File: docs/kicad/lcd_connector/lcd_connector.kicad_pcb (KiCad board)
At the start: 2 copper layers, 20.3 x 38.1 mm, 19 parts, among them J1 5V, J2 T_CS, J3 CLK, J4 MISO, J5 DC, J6 CS, J7 MOSI, J8 GND, M1 TFT_ILI9341

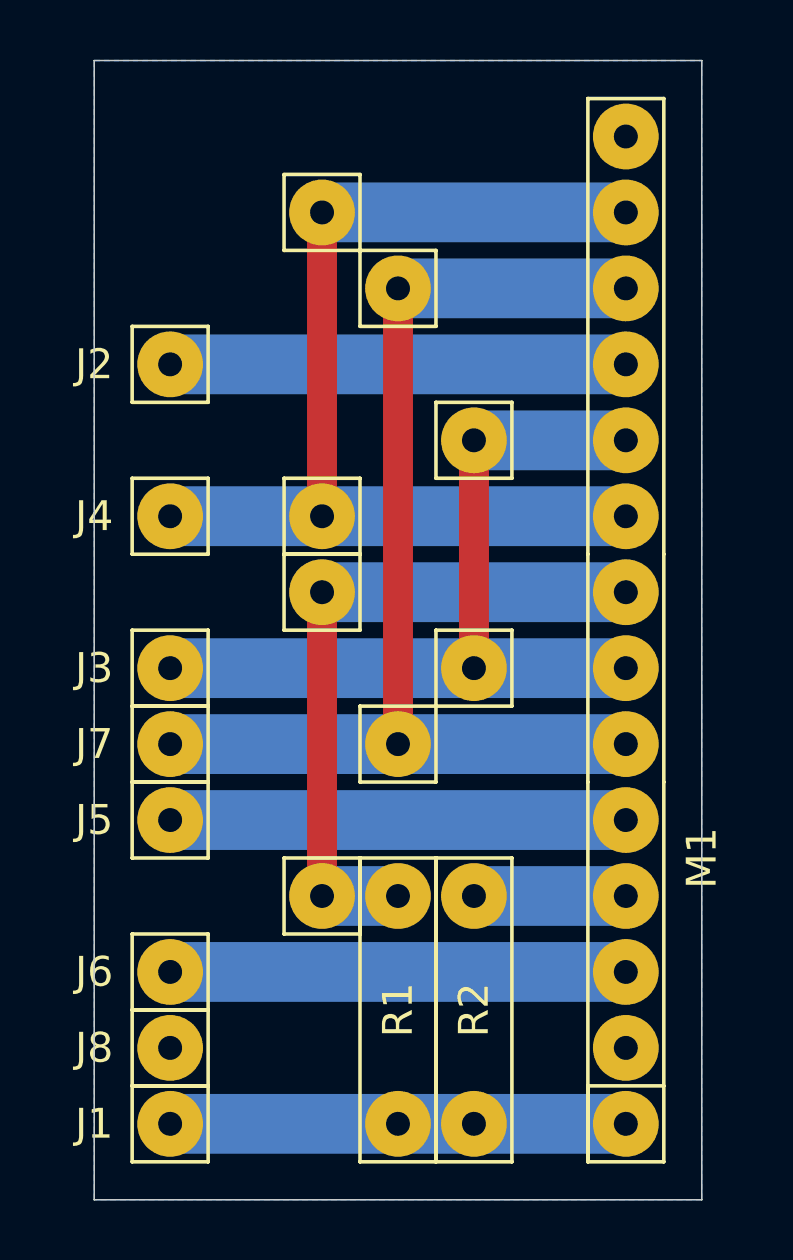
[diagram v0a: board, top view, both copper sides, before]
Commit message: kicad controller board v2.0 and smaller lcd_connector
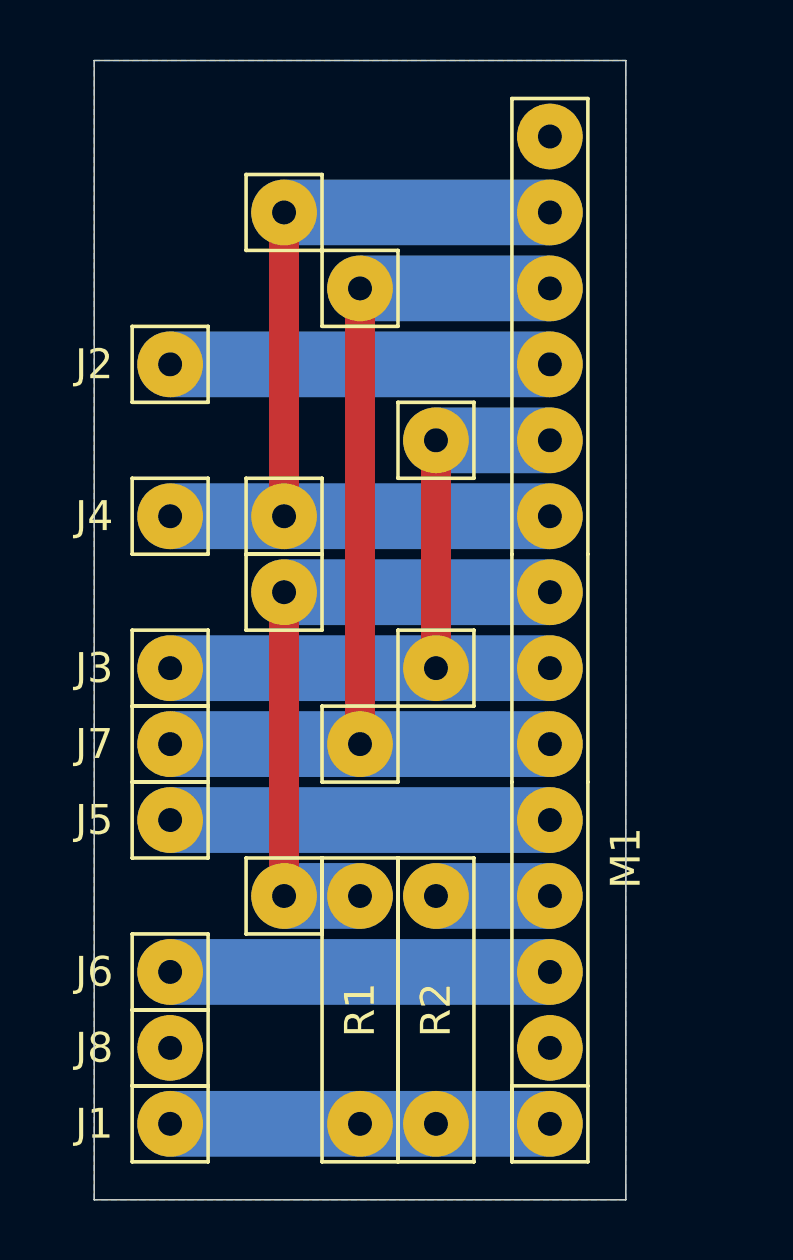
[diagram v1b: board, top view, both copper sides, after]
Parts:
- moved M1 2.54 mm to (15.2, -10.2)
- moved V1 1.27 mm to (6.35, -20.3)
- moved V2 1.27 mm to (6.35, -10.2)
- moved V6 1.27 mm to (6.35, -22.9)
- moved V8 1.27 mm to (6.35, -33.0)
- moved R1 1.27 mm to (8.89, -2.54)
- moved R2 1.27 mm to (11.4, -2.54)
- moved V3 1.27 mm to (11.4, -25.4)
- moved V5 1.27 mm to (11.4, -17.8)
- moved V7 1.27 mm to (8.89, -15.2)
- moved V9 1.27 mm to (8.89, -30.5)
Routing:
- net Net-(J3-Pad1): track 27.9 -> 24.1 mm
- net Net-(J7-Pad1): track 38.1 -> 34.3 mm
- net Net-(J4-Pad1): track 35.6 -> 31.8 mm
- net Net-(J6-Pad1): track 15.2 -> 12.7 mm
- net Net-(J5-Pad1): track 15.2 -> 12.7 mm
- net Net-(J2-Pad1): track 15.2 -> 12.7 mm
- net Net-(J1-Pad1): track 15.2 -> 12.7 mm
- net Net-(M1-Pad4): track 5.08 -> 3.81 mm
- net Net-(M1-Pad8): track 22.9 -> 21.6 mm
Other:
- board size 20.3 x 38.1 mm -> 17.8 x 38.1 mm
